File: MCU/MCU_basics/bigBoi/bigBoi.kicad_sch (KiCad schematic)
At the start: 25 parts, among them U1 STM32F469NIHx

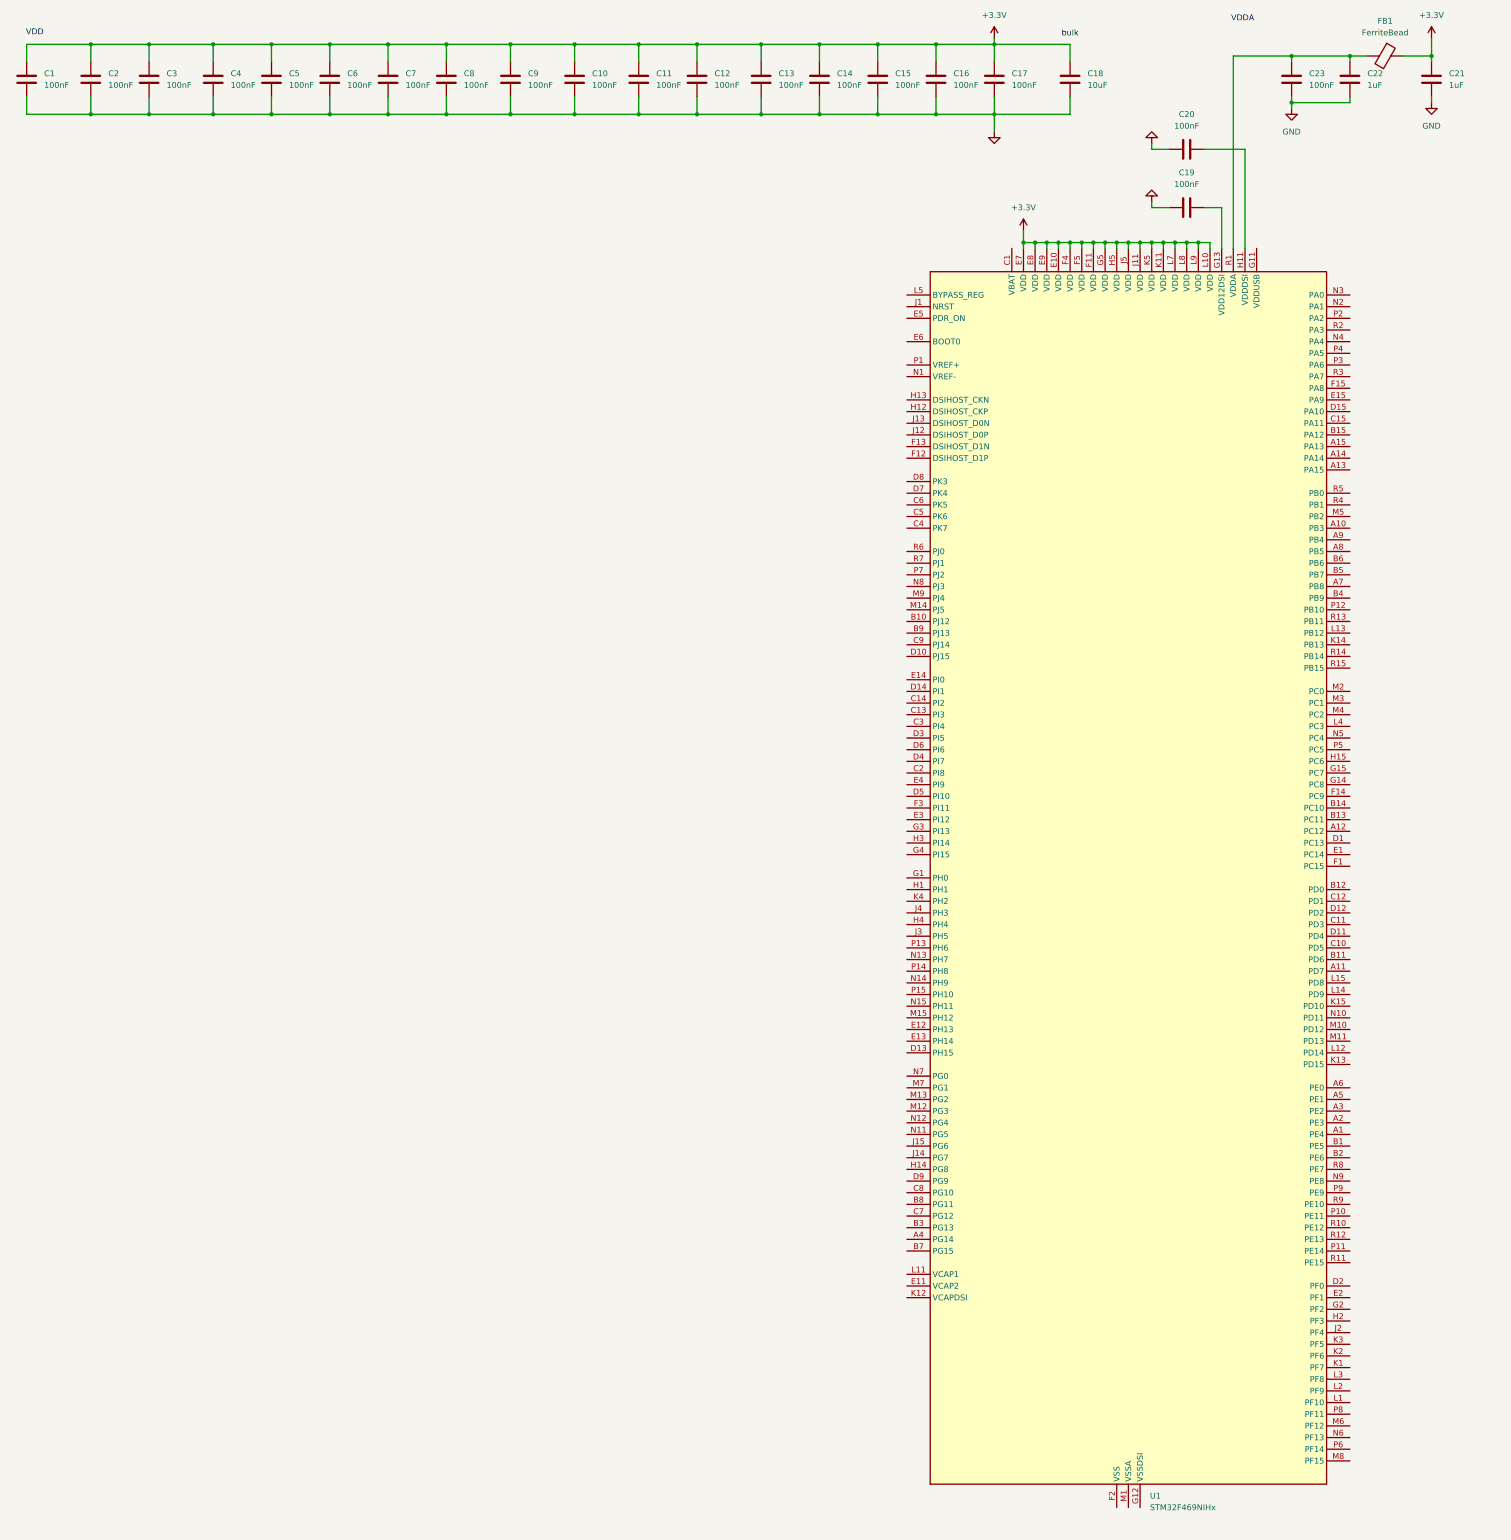
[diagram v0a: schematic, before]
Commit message: Power rails routed
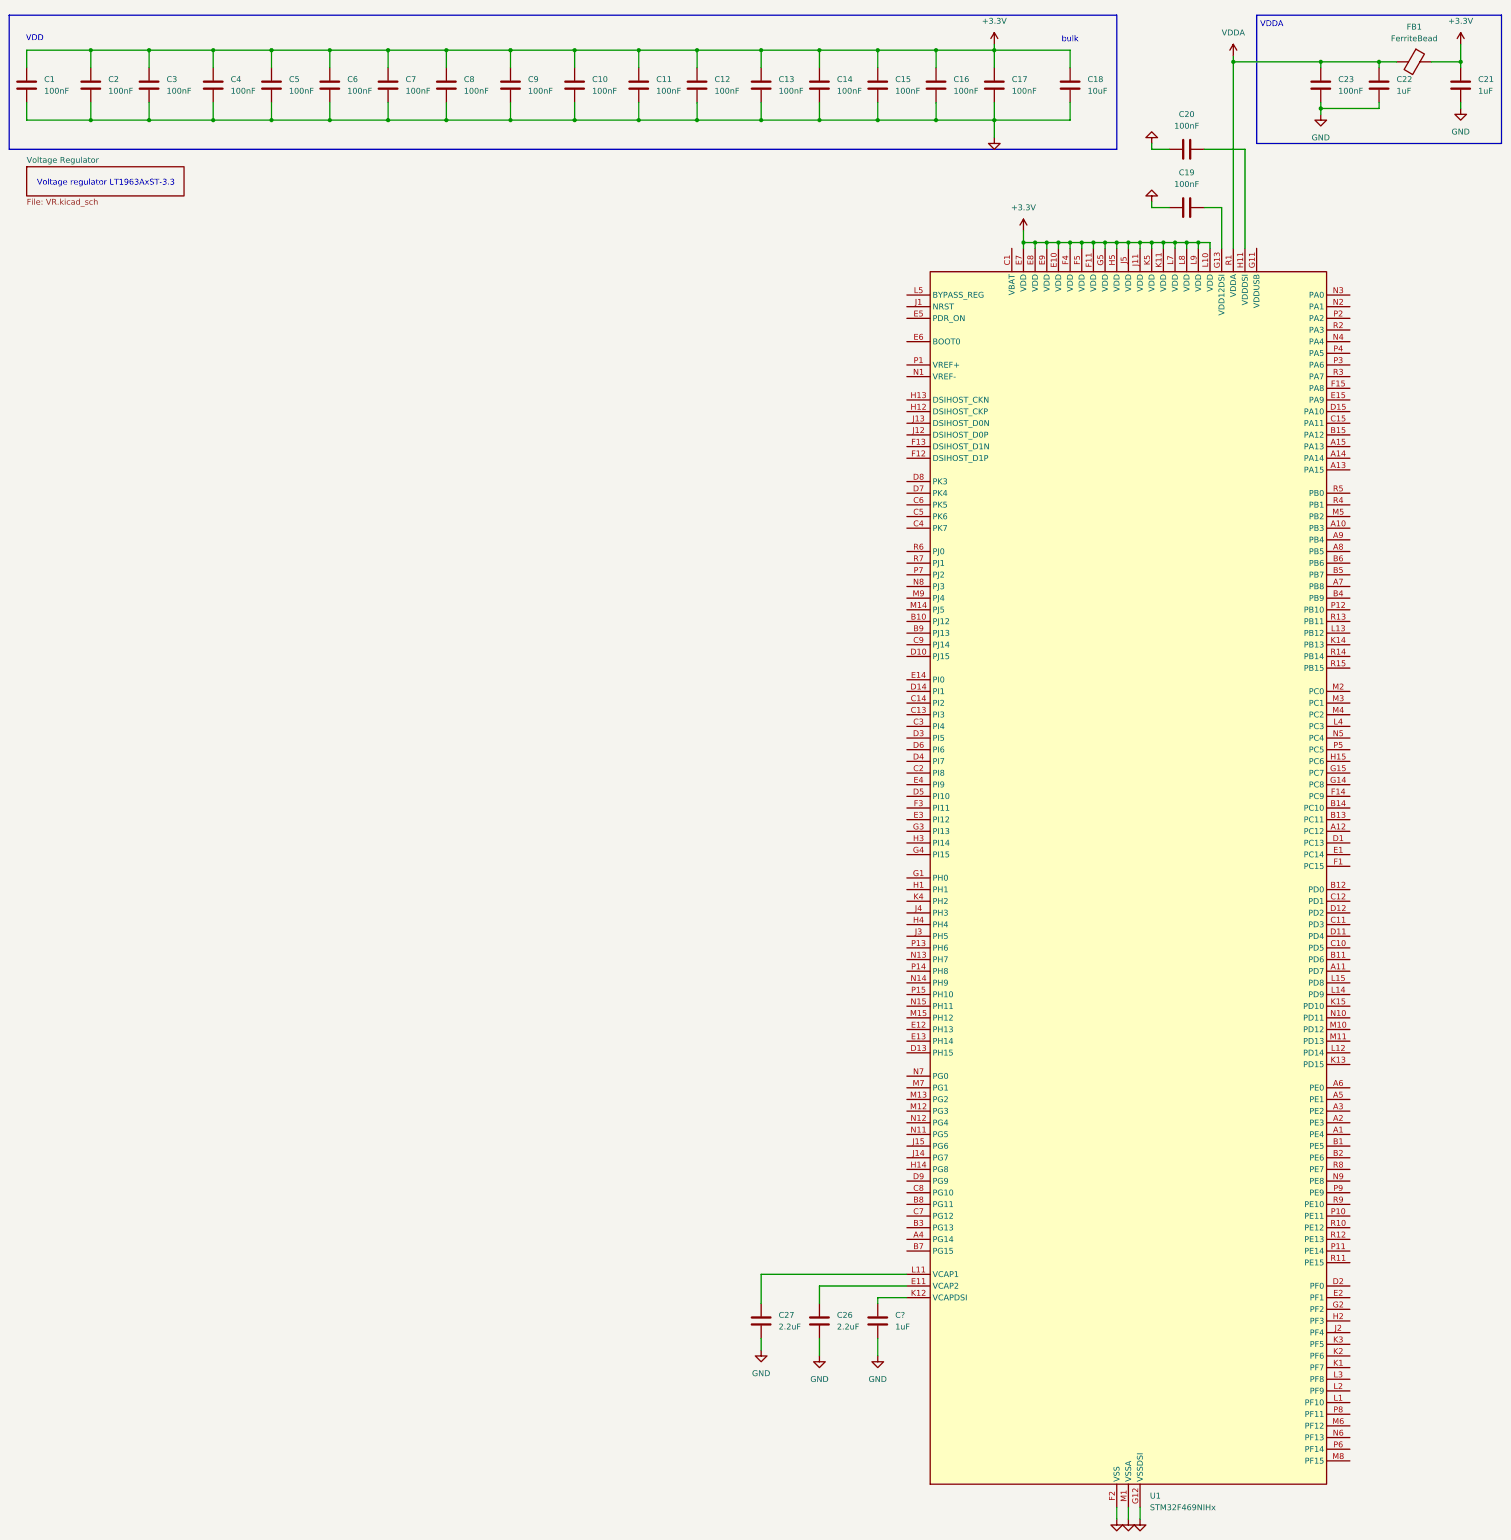
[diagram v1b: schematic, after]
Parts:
- added C26, C27: 2.2uF, symbol Device:C
- added C?: 1uF, symbol Device:C
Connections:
- net GND: now also U1.F10 (VSS), U1.F2 (VSS), U1.F6 (VSS), U1.F7 (VSS), U1.F8 (VSS), U1.F9 (VSS), U1.G10 (VSS), U1.G12 (VSSDSI), U1.G6 (VSS), U1.H10 (VSS), U1.H6 (VSS), U1.J10 (VSS), U1.J6 (VSS), U1.K10 (VSS), U1.K6 (VSS), U1.K7 (VSS), U1.K8 (VSS), U1.K9 (VSS), U1.L6 (VSS), U1.M1 (VSSA), C26.1, C27.2, C?.2
- net VDDA: now reaches C22.2, C23.2, FB1.2, U1.R1 (VDDA)
- net at U1.E11 (VCAP2): now also C26.2
- net at U1.K12 (VCAPDSI): now also C?.1
- net at U1.L11 (VCAP1): now also C27.1
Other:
- added sheet Voltage Regulator (VR.kicad_sch)
- note added: "Voltage regulator LT1963AxST-3.3"
- moved on the sheet: C1, C10, C11, C12, C13, C14, C15, C16, C17, C18, C2, C21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

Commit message: MCU small update
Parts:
- added C?: 1uF, symbol Device:C
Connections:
- net +3.3V: now also C?.1
- net SX1276_SCK_N: now reaches U1.A10 (PB3)
- net at U1.G11 (VDDUSB): now also C?.2
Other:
- added sheet SX1276 (radio.kicad_sch)
- note added: "SX1276 radio module"

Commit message: more power basics and comm
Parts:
- removed C19: 100nF, symbol Device:C
- removed C?: 1uF, symbol Device:C
- added C?: 10nF, symbol Device:C
- added C?: 1uF, symbol Device:C
- added C? (x2): C, symbol Device:C
- added C? (x3): 100nF, symbol Device:C
- added R?: 10k, symbol Device:R
- added SW1: Boot Switch, Button_Switch_SMD:SW_SPDT_PCM12, symbol Switch:SW_SPDT
- added Y?: 8MHz, symbol Device:Crystal_GND24
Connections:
- net +3.3V: now also U1.C1 (VBAT), U1.G11 (VDDUSB), C?.1, C?.1, C?.2, C?.2, SW1.3 (C)
- net GND: now also C?.2, U1.L5 (BYPASS_REG), U1.N1 (VREF-), C?.1, C?.2, C?.2, C?.2, SW1.1 (A), Y?.2 (G), Y?.4 (G)
- net DM3AT_MOSI_0: now reaches U1.A12 (PC12)
- net SWCLK: now reaches U1.A14 (PA14)
- net SWDIO: now reaches U1.A15 (PA13)
- net SX1276_MOSI_N: now reaches U1.A8 (PB5)
- net SX1276_MISO_N: now reaches U1.A9 (PB4)
- net DM3AT_MISO_N: now reaches U1.B13 (PC11)
- net DM3AT_SCLK_N: now reaches U1.B14 (PC10)
- net BNO086_SCLK_N: now reaches U1.C11 (PD3)
- net BNO086_MOSI_N: now reaches U1.C13 (PI3)
- net BNO086_MISO_N: now reaches U1.C14 (PI2)
- net at U1.E5 (PDR_ON): now also C?.2
- net at U1.E6 (BOOT0): now also R?.2
- net at U1.G1 (PH0): now also C?.1, Y?.1
- net VDSI: now reaches U1.G13 (VDD12DSI)
- net VDSI: now also U1.K12 (VCAPDSI)
- net at U1.H1 (PH1): now also C?.1, Y?.3
- net at U1.J1 (NRST): now also C?.2
- net at U1.P1 (VREF+): now also C?.1, C?.1
- new net: R?.1, SW1.2 (B)
- no-connect marks 0 -> 6
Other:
- added sheet BNO086 (IMU.kicad_sch)
- added sheet DM3AT (SD.kicad_sch)
- added sheet GPS (GPS.kicad_sch)
- note added: "Check load cap based on component"
- note added: "GPS module"
- note added: "Inertial measurement unit*"
- note added: "SD card"
- moved on the sheet: C18, C?

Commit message: Schematic pins assignment
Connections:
- net DM3AT_MISO_N: now also U1.A9 (PB4); no longer U1.B13 (PC11)
- net DM3AT_MOSI_0: now also U1.B11 (PD6); no longer U1.A12 (PC12)
- net DM3AT_SCLK_N: now also U1.A10 (PB3); no longer U1.B14 (PC10)
- net SX1276_MISO_N: now also U1.P3 (PA6); no longer U1.A9 (PB4)
- net SX1276_SCK_N: now also U1.P4 (PA5); no longer U1.A10 (PB3)
- net DM3AT_CS_N: now reaches U1.A11 (PD7)
- net PWM_TIM2CH1_SERVOPARA: now reaches U1.A13 (PA15)
- net EXT_SCLK: now reaches U1.A3 (PE2)
- net EXT_MISO: now reaches U1.B1 (PE5)
- net EXT_MOSI: now reaches U1.B2 (PE6)
- net BNO086_NRST_N: now reaches U1.C2 (PI8)
- net BNO086_INTN_N: now reaches U1.C3 (PI4)
- net GPS_RESET_N: now reaches U1.D1 (PC13)
- net BNO086_CSN_N: now reaches U1.D3 (PI5)
- net BNO086_BOOT_N: now reaches U1.D4 (PI7)
- net BNO086_CLKSEL_N: now reaches U1.D6 (PI6)
- net GPS_TIMEPULSE_N: now reaches U1.E1 (PC14)
- net BNO086_WAKE/PS0_N: now reaches U1.E4 (PI9)
- net PWM_TIM3CH2_FIN4: now reaches U1.G15 (PC7)
- net PWM_TIM3CH1_FIN3: now reaches U1.H15 (PC6)
- net DM3AT_CD_N: now reaches U1.L15 (PD8)
- net PWM_TIM3CH4_FIN2: now reaches U1.R4 (PB1)
- net PWM_TIM3CH3_FIN1: now reaches U1.R5 (PB0)
- new net GPS_RX_N: U1.B14 (PC10)
- new net GPS_TX_N: U1.B13 (PC11)
- new net GPS_WAKE_N: U1.A12 (PC12)
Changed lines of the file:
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@@
+	(wire
+		(pts
+			(xy 309.88 86.36) (xy 323.85 86.36)
+		)
+		(stroke
+			(width 0)
+			(type default)
+		)
+	)
 	(wire
 		(pts
@@
 	(wire
 		(pts
+			(xy 309.88 88.9) (xy 323.85 88.9)
+		)
+		(stroke
+			(width 0)
+			(type default)
+		)
+	)
+	(wire
+		(pts
 			(xy 207.01 20.32) (xy 207.01 24.13)
 		)
@@
 			(width 0)
 			(type default)
+		)
+	)
+	(label "BNO086_WAKE{slash}PS0_N"
+		(at 213.36 180.34 180)
+		(effects
+			(font
+				(size 1.27 1.27)
+			)
+			(justify right bottom)
+		)
+	)
+	(label "BNO086_CSN_N"
+		(at 213.36 170.18 180)
+		(effects
+			(font
+				(size 1.27 1.27)
+			)
+			(justify right bottom)
 		)
 	)
@@
 		)
 	)
+	(label "GPS_TX_N"
+		(at 309.88 187.96 0)
+		(effects
+			(font
+				(size 1.27 1.27)
+			)
+			(justify left bottom)
+		)
+	)
+	(label "BNO086_NRST_N"
+		(at 213.36 177.8 180)
+		(effects
+			(font
+				(size 1.27 1.27)
+			)
+			(justify right bottom)
+		)
+	)
 	(label "SWDIO"
 		(at 309.88 106.68 0)
@@
 		)
 	)
+	(label "EXT_MOSI"
+		(at 317.5 261.62 0)
+		(effects
+			(font
+				(size 1.27 1.27)
+			)
+			(justify left bottom)
+		)
+	)
 	(label "VDSI"
 		(at 207.01 292.1 270)
@@
 		)
 	)
-	(label "SX1276_SCK_N"
+	(label "EXT_SCLK"
+		(at 317.5 251.46 0)
+		(effects
+			(font
+				(size 1.27 1.27)
+			)
+			(justify left bottom)
+		)
+	)
+	(label "SX1276_MISO_N"
+		(at 323.85 88.9 0)
+		(effects
+			(font
+				(size 1.27 1.27)
+			)
+			(justify left bottom)
+		)
+	)
+	(label "SX1276_MOSI_N"
+		(at 328.93 129.54 0)
+		(effects
+			(font
+				(size 1.27 1.27)
+			)
+			(justify left bottom)
+		)
+	)
+	(label "PWM_TIM3CH4_FIN2"
+		(at 309.88 119.38 0)
+		(effects
+			(font
+				(size 1.27 1.27)
+			)
+			(justify left bottom)
+		)
+	)
+	(label "GPS_RESET_N"
+		(at 309.88 193.04 0)
+		(effects
+			(font
+				(size 1.27 1.27)
+			)
+			(justify left bottom)
+		)
+	)
+	(label "DM3AT_MOSI_0"
+		(at 309.88 218.44 0)
+		(effects
+			(font
+				(size 1.27 1.27)
+			)
+			(justify left bottom)
+		)
+	)
+	(label "PWM_TIM2CH1_SERVOPARA"
+		(at 309.88 111.76 0)
+		(effects
+			(font
+				(size 1.27 1.27)
+			)
+			(justify left bottom)
+		)
+	)
+	(label "GPS_WAKE_N"
+		(at 309.88 190.5 0)
+		(effects
+			(font
+				(size 1.27 1.27)
+			)
+			(justify left bottom)
+		)
+	)
+	(label "PWM_TIM3CH1_FIN3"
+		(at 309.88 175.26 0)
+		(effects
+			(font
+				(size 1.27 1.27)
+			)
+			(justify left bottom)
+		)
+	)
+	(label "BNO086_CLKSEL_N"
+		(at 213.36 172.72 180)
+		(effects
+			(font
+				(size 1.27 1.27)
+			)
+			(justify right bottom)
+		)
+	)
+	(label "DM3AT_SCLK_N"
 		(at 328.93 124.46 0)
 		(effects
@@
 		)
 	)
-	(label "DM3AT_MOSI_0"
-		(at 309.88 190.5 0)
-		(effects
-			(font
-				(size 1.27 1.27)
-			)
-			(justify left bottom)
-		)
-	)
-	(label "DM3AT_MISO_N"
-		(at 309.88 187.96 0)
-		(effects
-			(font
-				(size 1.27 1.27)
-			)
-			(justify left bottom)
+	(label "BNO086_INTN_N"
+		(at 213.36 167.64 180)
+		(effects
+			(font
+				(size 1.27 1.27)
+			)
+			(justify right bottom)
 		)
 	)
@@
 		)
 	)
+	(label "PWM_TIM3CH3_FIN1"
+		(at 309.88 116.84 0)
+		(effects
+			(font
+				(size 1.27 1.27)
+			)
+			(justify left bottom)
+		)
+	)
 	(label "VDSI"
 		(at 281.94 54.61 90)
@@
 		)
 	)
-	(label "SX1276_MOSI_N"
-		(at 328.93 129.54 0)
+	(label "GPS_TIMEPULSE_N"
+		(at 309.88 195.58 0)
+		(effects
+			(font
+				(size 1.27 1.27)
+			)
+			(justify left bottom)
+		)
+	)
+	(label "GPS_RX_N"
+		(at 309.88 185.42 0)
+		(effects
+			(font
+				(size 1.27 1.27)
+			)
+			(justify left bottom)
+		)
+	)
+	(label "SX1276_SCK_N"
+		(at 323.85 86.36 0)
+		(effects
+			(font
+				(size 1.27 1.27)
+			)
+			(justify left bottom)
+		)
+	)
+	(label "DM3AT_CS_N"
+		(at 309.88 220.98 0)
 		(effects
 			(font
@@
 		)
 	)
-	(label "DM3AT_SCLK_N"
-		(at 309.88 185.42 0)
-		(effects
-			(font
-				(size 1.27 1.27)
-			)
-			(justify left bottom)
-		)
-	)
-	(label "SX1276_MISO_N"
+	(label "DM3AT_MISO_N"
 		(at 328.93 127 0)
 		(effects
 			(font
+				(size 1.27 1.27)
+			)
+			(justify left bottom)
+		)
+	)
+	(label "BNO086_BOOT_N"
+		(at 213.36 175.26 180)
+		(effects
+			(font
+				(size 1.27 1.27)
+			)
+			(justify right bottom)
+		)
+	)
+	(label "PWM_TIM3CH2_FIN4"
+		(at 309.88 177.8 0)
+		(effects
+			(font
+				(size 1.27 1.27)
+			)
+			(justify left bottom)
+		)
+	)
+	(label "EXT_MISO"
+		(at 317.5 259.08 0)
+		(effects
+			(font
+				(size 1.27 1.27)
+			)
+			(justify left bottom)
+		)
+	)
+	(label "DM3AT_CD_N"
+		(at 309.88 223.52 0)
+		(effects
+			(font

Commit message: schematic connections
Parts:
- C14, C18: renamed from C?; value C -> 0402
- gave numbers to parts that had none: 8
- renumbered C11 to C12, C12 to C15, C13 to C16, C27 to C17, C14 to C20, C26 to C21, C15 to C23, C16 to C24, C17 to C25, C18 to C27, C20 to C28, C23 to C30, C22 to C31, C21 to C32
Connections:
- net BMP390_INT_N: now reaches U1.D14 (PI1)
- net BMP390_CS_N: now reaches U1.E14 (PI0)
- net SX1276_RESET_N: now reaches U1.E15 (PA9)
- net SX1276_NSS_N: now reaches U1.F15 (PA8)
- net SX1276_DI00_N: now reaches U1.R3 (PA7)
- net BNO086_MISO_N renamed BMP390_MISO_N
- net BNO086_MOSI_N renamed BMP390_MOSI_N
- net BNO086_SCLK_N renamed BMP390_SCK_N
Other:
- added sheet BMP390 (presTemp.kicad_sch)
- note added: "Barometer + thermometer"

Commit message: ERC resolving
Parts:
- removed C28: 100nF, symbol Device:C
- added J7: USB_B_Micro, Connector_USB:USB_Micro-B_Molex_47346-0001, symbol Connector:USB_B_Micro
- C1, C10, C11, C12, C13, C14, C15, C16, C18, C19, C2, C20, C22, C23, C24, C25, C26, C29, C3, C30, C31, C32, C4, C5, C6, C7, C8, C9: footprint (none) -> Capacitor_SMD:C_0402_1005Metric
- C17, C21: footprint (none) -> Capacitor_SMD:C_0603_1608Metric
- C27: footprint (none) -> Capacitor_SMD:C_0805_2012Metric
- FB1: value FerriteBead -> 120R; footprint (none) -> Inductor_SMD:L_0603_1608Metric
- R1: footprint (none) -> Resistor_SMD:R_0402_1005Metric
- Y1: footprint (none) -> Crystal:Crystal_SMD_3225-4Pin_3.2x2.5mm_HandSoldering
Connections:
- net +3.3V: now also U1.H11 (VDDDSI)
- net GND: now also J7.5 (GND)
- net at U1.B15 (PA12): now also J7.3 (D+)
- net at U1.C15 (PA11): now also J7.2 (D-)
- new net VBUS: J7.1 (VBUS)
- no-connect marks 6 -> 8
